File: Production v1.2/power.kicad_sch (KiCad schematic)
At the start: 18 parts, among them IC2 AP7375-33SA-7, U2 ADR02AUJZ-REEL7, U3 ADR06BUJZ-REEL7

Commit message: 1.2 routed
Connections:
- net +24V: no longer C23.2, C25.2, U2.3 (VIN), U3.3 (VIN)
- net GND: no longer C19.2, C20.2, C21.2, C22.1, C23.1, C24.1, C25.1, U2.2 (GND), U3.2 (GND)
- net GNDANA: now also C19.2, C20.2, C21.2, C22.1, C23.1, C24.1, C25.1, U2.2 (GND), U3.2 (GND)
- net VIN: now also C23.2, C25.2, U2.3 (VIN), U3.3 (VIN)

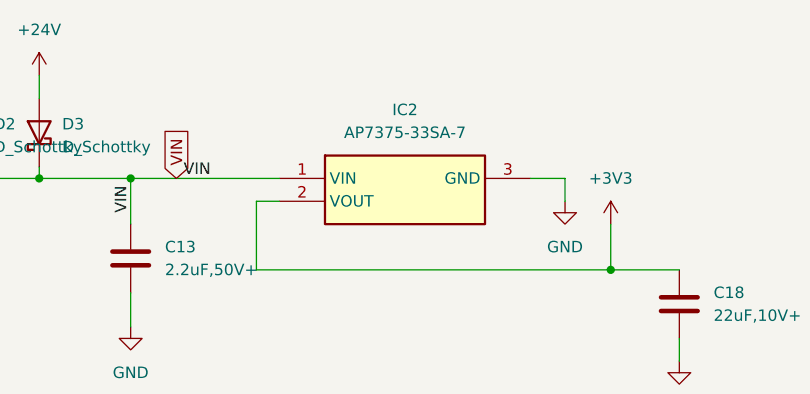
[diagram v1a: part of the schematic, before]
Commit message: v1.2 checked & labeled
flipped fpc connector to underside, for better ribbon routing.
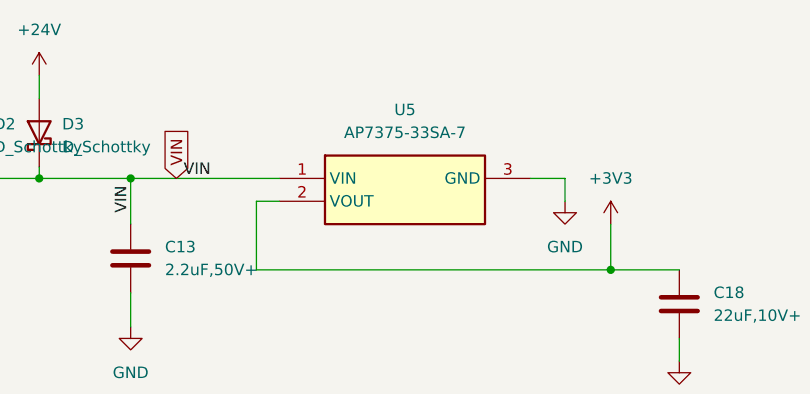
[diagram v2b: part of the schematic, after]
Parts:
- renumbered IC2 to U5
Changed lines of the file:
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@@
 		(dnp no)
 		(fields_autoplaced yes)
-		(property "Reference" "#PWR031"
+		(property "Reference" "#PWR029"
 			(at 40.64 58.42 0)
 			(effects
@@
 			(project "Production v1.2"
 				(path "/36880c03-5560-4777-bc12-f18c70ba2db4/221e7a9c-c1e1-4a96-93ff-c7863ac19137"
-					(reference "#PWR031")
+					(reference "#PWR029")
 					(unit 1)
 				)
@@
 		(dnp no)
 		(fields_autoplaced yes)
-		(property "Reference" "IC2"
+		(property "Reference" "U5"
 			(at 71.12 27.94 0)
 			(effects
@@
 			(project "Production v1.2"
 				(path "/36880c03-5560-4777-bc12-f18c70ba2db4/221e7a9c-c1e1-4a96-93ff-c7863ac19137"
-					(reference "IC2")
+					(reference "U5")
 					(unit 1)
 				)
@@
 		(dnp no)
 		(fields_autoplaced yes)
-		(property "Reference" "#PWR029"
+		(property "Reference" "#PWR027"
 			(at 22.86 27.94 0)
 			(effects
@@
 			(project "Production v1.2"
 				(path "/36880c03-5560-4777-bc12-f18c70ba2db4/221e7a9c-c1e1-4a96-93ff-c7863ac19137"
-					(reference "#PWR029")
+					(reference "#PWR027")
 					(unit 1)
 				)
@@
 		(dnp no)
 		(fields_autoplaced yes)
-		(property "Reference" "#PWR033"
+		(property "Reference" "#PWR031"
 			(at 54.61 111.76 0)
 			(effects
@@
 			(project "Production v1.2"
 				(path "/36880c03-5560-4777-bc12-f18c70ba2db4/221e7a9c-c1e1-4a96-93ff-c7863ac19137"
-					(reference "#PWR033")
+					(reference "#PWR031")
 					(unit 1)
 				)
@@
 		(dnp no)
 		(fields_autoplaced yes)
-		(property "Reference" "#PWR036"
+		(property "Reference" "#PWR034"
 			(at 101.6 62.23 0)
 			(effects
@@
 			(project "Production v1.2"
 				(path "/36880c03-5560-4777-bc12-f18c70ba2db4/221e7a9c-c1e1-4a96-93ff-c7863ac19137"
-					(reference "#PWR036")
+					(reference "#PWR034")
 					(unit 1)
 				)
@@
 		(dnp no)
 		(fields_autoplaced yes)
-		(property "Reference" "#PWR032"
+		(property "Reference" "#PWR030"
 			(at 54.61 92.71 0)
 			(effects
@@
 			(project "Production v1.2"
 				(path "/36880c03-5560-4777-bc12-f18c70ba2db4/221e7a9c-c1e1-4a96-93ff-c7863ac19137"
-					(reference "#PWR032")
+					(reference "#PWR030")
 					(unit 1)
 				)
@@
 		(dnp no)
 		(fields_autoplaced yes)
-		(property "Reference" "#PWR035"
+		(property "Reference" "#PWR033"
 			(at 93.98 44.45 0)
 			(effects
@@
 			(project "Production v1.2"
 				(path "/36880c03-5560-4777-bc12-f18c70ba2db4/221e7a9c-c1e1-4a96-93ff-c7863ac19137"
-					(reference "#PWR035")
+					(reference "#PWR033")
 					(unit 1)
 				)
@@
 		(dnp no)
 		(fields_autoplaced yes)
-		(property "Reference" "#PWR034"
+		(property "Reference" "#PWR032"
 			(at 88.9 44.45 0)
 			(effects
@@
 			(project "Production v1.2"
 				(path "/36880c03-5560-4777-bc12-f18c70ba2db4/221e7a9c-c1e1-4a96-93ff-c7863ac19137"
-					(reference "#PWR034")
+					(reference "#PWR032")
 					(unit 1)
 				)
@@
 		(dnp no)
 		(fields_autoplaced yes)
-		(property "Reference" "#PWR030"
+		(property "Reference" "#PWR028"
 			(at 30.48 27.94 0)
 			(effects
@@
 			(project "Production v1.2"
 				(path "/36880c03-5560-4777-bc12-f18c70ba2db4/221e7a9c-c1e1-4a96-93ff-c7863ac19137"
-					(reference "#PWR030")
-					(unit 1)
-				)
+					(reference "#PWR028")
+					(unit 1)
+				)

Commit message: Final tweaks for production v1.2, as manufactured
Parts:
- C13: value 2.2uF,50V+ -> 2.2uF,100V
- C14, C16: Part Number CL05C010CB5NNNC -> GRM155R61A106ME11D; URL https://www.digikey.com/en/products/detail/samsung-electro-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 -> https://www.digikey.com/en/products/detail/murata-electroni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
- C15, C17, C20, C21: Part Number CL05C010CB5NNNC -> CL05B104KA5NNNC; URL https://www.digikey.com/en/products/detail/samsung-electro-mechanics/CL05C010CB5NNNC/3887253 -> https://www.digikey.com/en/products/detail/samsung-electro-mechanics/CL05B104KA5NNNC/5961204
- C19: Part Number CL05C010CB5NNNC -> CL05A475MP5NRNC; URL https://www.digikey.com/en/products/detail/samsung-electro-mechanics/CL05C010CB5NNNC/3887253 -> https://www.digikey.com/en/products/detail/samsung-electro-mechanics/CL05A475MP5NRNC/3887140
- C22, C24: Part Number GRM158R61A226ME15D -> CL05B104KP5NNNC; URL https://www.digikey.com/en/products/detail/murata-electroni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 -> https://www.digikey.com/en/products/detail/samsung-electro-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
- C23, C25: value .1uF, 50V -> .1uF, 100V; Part Number C2012X7R2A225K125AC -> CL21B104KCFNNNE; URL https://www.digikey.com/en/products/detail/tdk-corporation/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 -> https://www.digikey.com/en/products/detail/samsung-electro-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
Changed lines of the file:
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@@
 			)
 		)
-		(property "Part Number" "CL05C010CB5NNNC"
+		(property "Part Number" "CL05B104KA5NNNC"
 			(at 125.73 97.79 0)
 			(effects
@@
 			)
 		)
-		(property "URL" "https://www.digikey.com/en/products/detail/samsung-electro-mechanics/CL05C010CB5NNNC/3887253"
+		(property "URL" "https://www.digikey.com/en/products/detail/samsung-electro-mechanics/CL05B104KA5NNNC/5961204"
 			(at 125.73 97.79 0)
 			(effects
@@
 			)
 		)
-		(property "Part Number" "CL05C010CB5NNNC"
+		(property "Part Number" "CL05B104KA5NNNC"
 			(at 115.57 97.79 0)
 			(effects
@@
 			)
 		)
-		(property "URL" "https://www.digikey.com/en/products/detail/samsung-electro-mechanics/CL05C010CB5NNNC/3887253"
+		(property "URL" "https://www.digikey.com/en/products/detail/samsung-electro-mechanics/CL05B104KA5NNNC/5961204"
 			(at 115.57 97.79 0)
 			(effects
@@
 			)
 		)
-		(property "Part Number" "CL05C010CB5NNNC"
+		(property "Part Number" "CL05B104KA5NNNC"
 			(at 59.69 97.79 0)
 			(effects
@@
 			)
 		)
-		(property "URL" "https://www.digikey.com/en/products/detail/samsung-electro-mechanics/CL05C010CB5NNNC/3887253"
+		(property "URL" "https://www.digikey.com/en/products/detail/samsung-electro-mechanics/CL05B104KA5NNNC/5961204"
 			(at 59.69 97.79 0)
 			(effects
@@
 			)
 		)
-		(property "Value" ".1uF, 50V"
+		(property "Value" ".1uF, 100V"
 			(at 195.58 59.69 90)
 			(effects
@@
 			)
 		)
-		(property "Part Number" "C2012X7R2A225K125AC"
+		(property "Part Number" "CL21B104KCFNNNE"
 			(at 195.58 64.77 0)
 			(effects
@@
 			)
 		)
-		(property "URL" "https://www.digikey.com/en/products/detail/tdk-corporation/C2012X7R2A225K125AC/20482638"
+		(property "URL" "https://www.digikey.com/en/products/detail/samsung-electro-mechanics/CL21B104KCFNNNE/5961324"
 			(at 195.58 64.77 0)
 			(effects
@@
 			)
 		)
-		(property "Datasheet" "https://www.diodes.com/assets/Datasheets/AP7375.pdf"
+		(property "Datasheet" ""
 			(at 81.28 230.48 0)
 			(effects
@@
 			)
 		)
-		(property "Datasheet" "~"
+		(property "Datasheet" ""
 			(at 74.93 97.79 0)
 			(effects
@@
 			)
 		)
-		(property "Part Number" "CL05C010CB5NNNC"
+		(property "Part Number" "GRM155R61A106ME11D"
 			(at 74.93 97.79 0)
 			(effects
@@
 			)
 		)
-		(property "URL" "https://www.digikey.com/en/products/detail/samsung-electro-mechanics/CL05C010CB5NNNC/3887253"
+		(property "URL" "https://www.digikey.com/en/products/detail/murata-electronics/GRM155R61A106ME11D/12091056"
 			(at 74.93 97.79 0)
 			(effects
@@
 			)
 		)
-		(property "Part Number" "CL05C010CB5NNNC"
+		(property "Part Number" "CL05A475MP5NRNC"
 			(at 104.14 97.79 0)
 			(effects
@@
 			)
 		)
-		(property "URL" "https://www.digikey.com/en/products/detail/samsung-electro-mechanics/CL05C010CB5NNNC/3887253"
+		(property "URL" "https://www.digikey.com/en/products/detail/samsung-electro-mechanics/CL05A475MP5NRNC/3887140"
 			(at 104.14 97.79 0)
 			(effects
@@
 			)
 		)
-		(property "Part Number" "CL05C010CB5NNNC"
+		(property "Part Number" "CL05B104KA5NNNC"
 			(at 86.36 97.79 0)
 			(effects
@@
 			)
 		)
-		(property "URL" "https://www.digikey.com/en/products/detail/samsung-electro-mechanics/CL05C010CB5NNNC/3887253"
+		(property "URL" "https://www.digikey.com/en/products/detail/samsung-electro-mechanics/CL05B104KA5NNNC/5961204"
 			(at 86.36 97.79 0)
 			(effects
@@
 			)
 		)
-		(property "Value" "2.2uF,50V+"
+		(property "Value" "2.2uF,100V"
 			(at 44.45 45.7199 0)
 			(effects
@@
 			)
 		)
-		(property "Value" ".1uF, 50V"
+		(property "Value" ".1uF, 100V"
 			(at 262.89 58.42 90)
 			(effects
@@
 			)
 		)
-		(property "Part Number" "C2012X7R2A225K125AC"
+		(property "Part Number" "CL21B104KCFNNNE"
 			(at 262.89 63.5 0)
 			(effects
@@
 			)
 		)
-		(property "URL" "https://www.digikey.com/en/products/detail/tdk-corporation/C2012X7R2A225K125AC/20482638"
+		(property "URL" "https://www.digikey.com/en/products/detail/samsung-electro-mechanics/CL21B104KCFNNNE/5961324"
 			(at 262.89 63.5 0)
 			(effects
@@
 			)
 		)
-		(property "Datasheet" "~"
+		(property "Datasheet" ""
 			(at 48.26 97.79 0)
 			(effects
@@
 			)
 		)
-		(property "Part Number" "CL05C010CB5NNNC"
+		(property "Part Number" "GRM155R61A106ME11D"
 			(at 48.26 97.79 0)
 			(effects
@@
 			)
 		)
-		(property "URL" "https://www.digikey.com/en/products/detail/samsung-electro-mechanics/CL05C010CB5NNNC/3887253"
+		(property "URL" "https://www.digikey.com/en/products/detail/murata-electronics/GRM155R61A106ME11D/12091056"
 			(at 48.26 97.79 0)
 			(effects
@@
 			)
 		)
-		(property "Part Number" "GRM158R61A226ME15D"
+		(property "Part Number" "CL05B104KP5NNNC"
 			(at 257.81 38.1 0)
 			(effects
@@
 			)
 		)
-		(property "URL" "https://www.digikey.com/en/products/detail/murata-electronics/GRM158R61A226ME15D/16033379"
+		(property "URL" "https://www.digikey.com/en/products/detail/samsung-electro-mechanics/CL05B104KP5NNNC/3886660"
 			(at 257.81 38.1 0)
 			(effects
@@
 			)
 		)
-		(property "Part Number" "GRM158R61A226ME15D"
+		(property "Part Number" "CL05B104KP5NNNC"
 			(at 190.5 39.37 0)
 			(effects
@@
 			)
 		)
-		(property "URL" "https://www.digikey.com/en/products/detail/murata-electronics/GRM158R61A226ME15D/16033379"
+		(property "URL" "https://www.digikey.com/en/products/detail/samsung-electro-mechanics/CL05B104KP5NNNC/3886660"
 			(at 190.5 39.37 0)
 			(effects
@@
 			)
 		)
-		(property "Datasheet" "ADR02AUJZ-REEL7"
+		(property "Datasheet" ""
 			(at 151.13 59.69 0)
 			(effects
@@
 			)
 		)
-		(property "Datasheet" "ADR06BUJZ-REEL7"
+		(property "Datasheet" ""
 			(at 218.44 58.42 0)
 			(effects
